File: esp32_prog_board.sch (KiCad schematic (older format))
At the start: 21 parts, among them J1 105450-0101, J2 S6B-PH-SM4-TB, Q1 MMDT2222A, SW1 PTS810, U1 SP3401, U2 AP2112K-3.3, U3 CP2104

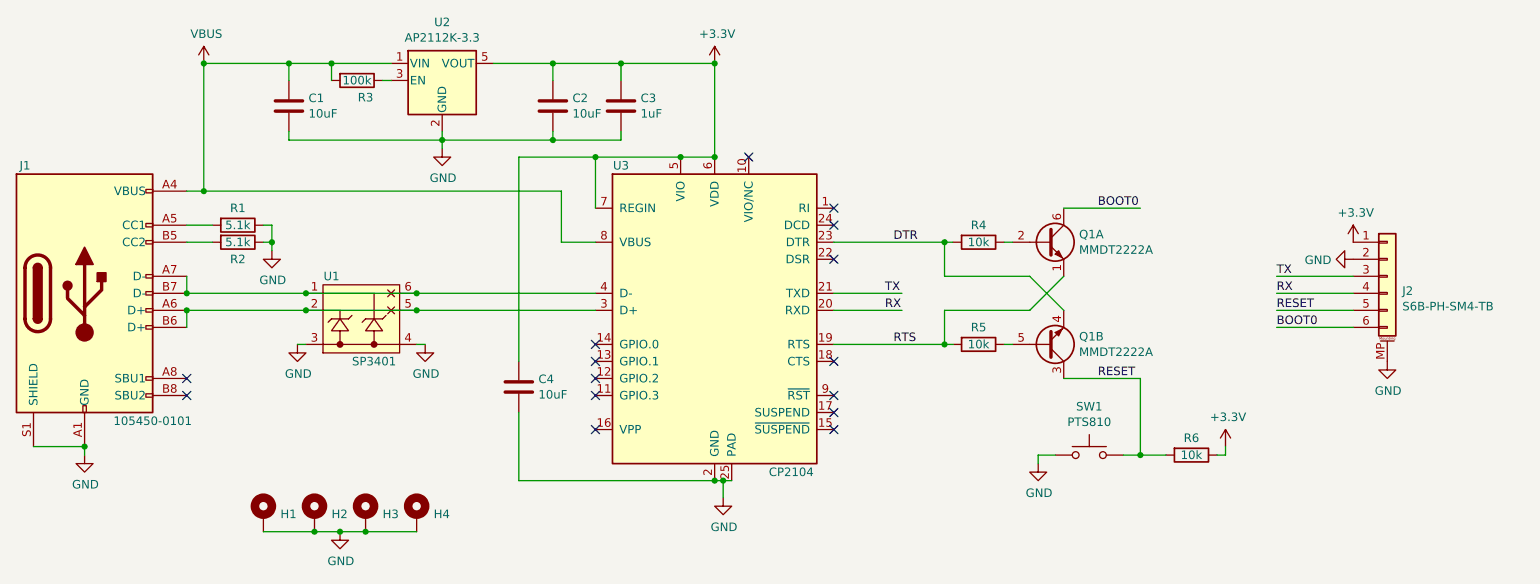
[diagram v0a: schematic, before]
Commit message: Added VBUS ESD, and TX/RX/PWR LEDs
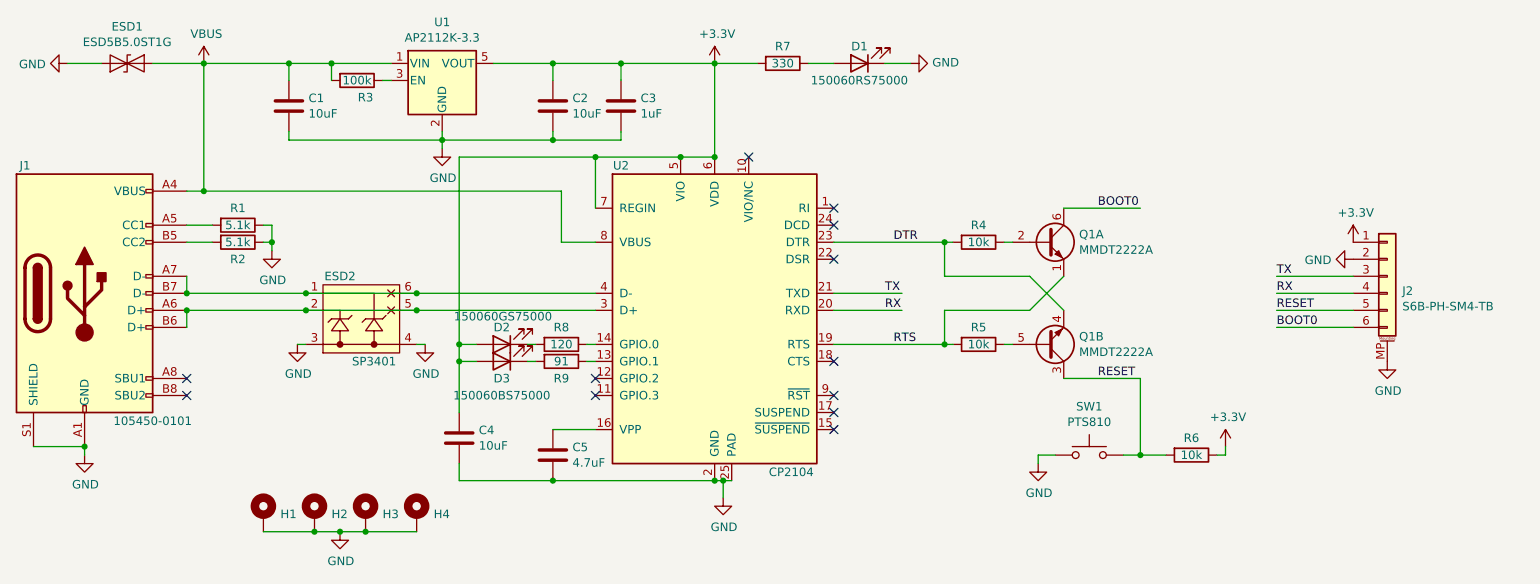
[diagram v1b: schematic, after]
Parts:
- added C5: 4.7uF, Resistor_SMD:R_0603_1608Metric, symbol Device:C
- added D1: 150060RS75000, LED_SMD:LED_0603_1608Metric, symbol Device:LED
- added D2: 150060GS75000, LED_SMD:LED_0603_1608Metric, symbol Device:LED
- added D3: 150060BS75000, LED_SMD:LED_0603_1608Metric, symbol Device:LED
- added ESD1: ESD5B5.0ST1G, Diode_SMD:D_SOD-523, symbol Diode:ESD9B5.0ST5G
- added R7: 330, Resistor_SMD:R_0603_1608Metric, symbol Device:R
- added R8: 120, Resistor_SMD:R_0603_1608Metric, symbol Device:R
- added R9: 91, Resistor_SMD:R_0603_1608Metric, symbol Device:R
- renumbered U1 to ESD2, U2 to U1, U3 to U2
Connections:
- wire segments 84 -> 99
- no-connect marks 15 -> 12
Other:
- moved on the sheet: C4
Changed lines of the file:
@@
 $EndDescr
 $Comp
-L Interface_USB:CP2104 U3
+L Interface_USB:CP2104 U2
 U 1 1 5F29D50C
 P 6000 3750
-F 0 "U3" H 5450 4600 50  0000 C CNN
+F 0 "U2" H 5450 4600 50  0000 C CNN
 F 1 "CP2104" H 6450 2800 50  0000 C CNN
 F 2 "Package_DFN_QFN:QFN-24-1EP_4x4mm_P0.5mm_EP2.6x2.6mm" H 6150 2800 50  0001 L CNN
@@
 NoConn ~ 6700 4350
 NoConn ~ 6700 4450
-NoConn ~ 5300 4450
 NoConn ~ 5300 4250
 NoConn ~ 5300 4150
-NoConn ~ 5300 4050
-NoConn ~ 5300 3950
-$Comp
-L Device:C C4
-U 1 1 5F2B6E8C
-P 4850 4200
-F 0 "C4" H 4965 4246 50  0000 L CNN
-F 1 "10uF" H 4965 4155 50  0000 L CNN
-F 2 "Resistor_SMD:R_0603_1608Metric" H 4888 4050 50  0001 C CNN
-F 3 "~" H 4850 4200 50  0001 C CNN
-	1    4850 4200
-	1    0    0    -1
-$EndComp
-Wire Wire Line
-	4850 4350 4850 4750
-Wire Wire Line
-	4850 4750 6000 4750
 Connection ~ 6000 4750
-Wire Wire Line
-	4850 4050 4850 2850
-Wire Wire Line
-	4850 2850 5300 2850
-Connection ~ 5300 2850
 $Comp
 L power:+3.3V #PWR?
@@
 $EndComp
 Wire Wire Line
-	5100 3050 5100 3350
-Wire Wire Line
-	5100 3350 5300 3350
-Wire Wire Line
 	2900 3050 3000 3050
 Wire Wire Line
 	3000 2300 3000 3050
-Wire Wire Line
-	3000 3050 5100 3050
 Connection ~ 3000 3050
 $Comp
-L LittelFuse:SP3401 U1
+L LittelFuse:SP3401 ESD2
 U 1 1 5F2B5D60
 P 3900 3650
-F 0 "U1" H 3750 3750 50  0000 C CNN
+F 0 "ESD2" H 3800 3750 50  0000 C CNN
 F 1 "SP3401" H 4000 3250 50  0000 C CNN
 F 2 "LittelFuse:SP3401" H 3900 3200 50  0001 C CNN
@@
 RESET
 $Comp
-L Regulator_Linear:AP2112K-3.3 U2
+L Regulator_Linear:AP2112K-3.3 U1
 U 1 1 5F2CF8DA
 P 4400 2400
-F 0 "U2" H 4400 2742 50  0000 C CNN
+F 0 "U1" H 4400 2742 50  0000 C CNN
 F 1 "AP2112K-3.3" H 4400 2651 50  0000 C CNN
 F 2 "Package_TO_SOT_SMD:SOT-23-5" H 4400 2725 50  0001 C CNN
@@
 Wire Wire Line
 	9300 3850 9750 3850
+Connection ~ 5300 2850
+Wire Wire Line
+	3000 3050 5100 3050
+Wire Wire Line
+	5100 3350 5300 3350
+Wire Wire Line
+	5100 3050 5100 3350
+$Comp
+L Device:C C4
+U 1 1 5F2B6E8C
+P 4500 4500
+F 0 "C4" H 4615 4546 50  0000 L CNN
+F 1 "10uF" H 4615 4455 50  0000 L CNN
+F 2 "Resistor_SMD:R_0603_1608Metric" H 4538 4350 50  0001 C CNN
+F 3 "~" H 4500 4500 50  0001 C CNN
+	1    4500 4500
+	1    0    0    -1
+$EndComp
+Wire Wire Line
+	4500 4650 4500 4750
+Wire Wire Line
+	4500 4350 4500 4050
+Wire Wire Line
+	4500 2850 5300 2850
+$Comp
+L Device:C C5
+U 1 1 5F2F6677
+P 5050 4600
+F 0 "C5" H 5165 4646 50  0000 L CNN
+F 1 "4.7uF" H 5165 4555 50  0000 L CNN
+F 2 "Resistor_SMD:R_0603_1608Metric" H 5088 4450 50  0001 C CNN
+F 3 "~" H 5050 4600 50  0001 C CNN
+	1    5050 4600
+	1    0    0    -1
+$EndComp
+Wire Wire Line
+	4500 4750 5050 4750
+Wire Wire Line
+	5050 4750 6000 4750
+Connection ~ 5050 4750
+Wire Wire Line
+	5050 4450 5300 4450
+$Comp
+L Diode:ESD9B5.0ST5G ESD1
+U 1 1 5F2A4472
+P 2550 2300
+F 0 "ESD1" H 2550 2516 50  0000 C CNN
+F 1 "ESD5B5.0ST1G" H 2550 2425 50  0000 C CNN
+F 2 "Diode_SMD:D_SOD-523" H 2550 2300 50  0001 C CNN
+F 3 "" H 2550 2300 50  0001 C CNN
+	1    2550 2300
+	1    0    0    -1
+$EndComp
+$Comp
+L power:GND #PWR?
+U 1 1 5F2AC941
+P 2200 2300
+F 0 "#PWR?" H 2200 2050 50  0001 C CNN
+F 1 "GND" V 2205 2172 50  0000 R CNN
+F 2 "" H 2200 2300 50  0001 C CNN
+F 3 "" H 2200 2300 50  0001 C CNN
+	1    2200 2300
+	0    1    1    0
+$EndComp
+Wire Wire Line
+	2200 2300 2400 2300
+Wire Wire Line
+	2700 2300 3000 2300
+$Comp
+L Device:R R7
+U 1 1 5F2B9ABB
+P 6400 2300
+F 0 "R7" V 6300 2300 50  0000 C CNN
+F 1 "330" V 6400 2300 50  0000 C CNN
+F 2 "Resistor_SMD:R_0603_1608Metric" V 6330 2300 50  0001 C CNN
+F 3 "~" H 6400 2300 50  0001 C CNN
+	1    6400 2300
+	0    1    1    0
+$EndComp
+$Comp
+L Device:R R8
+U 1 1 5F2BA0DD
+P 5100 3950
+F 0 "R8" V 5000 3950 50  0000 C CNN
+F 1 "120" V 5100 3950 50  0000 C CNN
+F 2 "Resistor_SMD:R_0603_1608Metric" V 5030 3950 50  0001 C CNN
+F 3 "~" H 5100 3950 50  0001 C CNN
+	1    5100 3950
+	0    1    1    0
+$EndComp
+$Comp
+L Device:R R9
+U 1 1 5F2BA7D1
+P 5100 4050
+F 0 "R9" V 5200 4050 50  0000 C CNN
+F 1 "91" V 5100 4050 50  0000 C CNN
+F 2 "Resistor_SMD:R_0603_1608Metric" V 5030 4050 50  0001 C CNN
+F 3 "~" H 5100 4050 50  0001 C CNN
+	1    5100 4050
+	0    1    1    0
+$EndComp
+Wire Wire Line
+	6000 2300 6250 2300
+$Comp
+L Device:LED D1
+U 1 1 5F2C4AFE
+P 6850 2300
+F 0 "D1" H 6850 2200 50  0000 C CNN
+F 1 "150060RS75000" H 6850 2400 50  0000 C CNN
+F 2 "LED_SMD:LED_0603_1608Metric" H 6850 2300 50  0001 C CNN
+F 3 "~" H 6850 2300 50  0001 C CNN
+	1    6850 2300
+	-1   0    0    1
+$EndComp
+$Comp
+L power:GND #PWR?
+U 1 1 5F2C65F7
+P 7150 2300
+F 0 "#PWR?" H 7150 2050 50  0001 C CNN
+F 1 "GND" V 7155 2172 50  0000 R CNN
+F 2 "" H 7150 2300 50  0001 C CNN
+F 3 "" H 7150 2300 50  0001 C CNN
+	1    7150 2300
+	0    -1   -1   0
+$EndComp
+Wire Wire Line
+	6550 2300 6700 2300
+Wire Wire Line
+	7000 2300 7150 2300
+Wire Wire Line
+	5250 3950 5300 3950
+Wire Wire Line
+	5250 4050 5300 4050
+$Comp
+L Device:LED D2
+U 1 1 5F2DAF7D
+P 4750 3950
+F 0 "D2" H 4750 3850 50  0000 C CNN
+F 1 "150060GS75000" H 4743 3786 50  0000 C CNN
+F 2 "LED_SMD:LED_0603_1608Metric" H 4750 3950 50  0001 C CNN
+F 3 "~" H 4750 3950 50  0001 C CNN
+	1    4750 3950
+	-1   0    0    1
+$EndComp
+$Comp
+L Device:LED D3
+U 1 1 5F2DB7FA
+P 4750 4050
+F 0 "D3" H 4750 4150 50  0000 C CNN
+F 1 "150060BS75000" H 4750 4250 50  0000 C CNN
+F 2 "LED_SMD:LED_0603_1608Metric" H 4750 4050 50  0001 C CNN
+F 3 "~" H 4750 4050 50  0001 C CNN
+	1    4750 4050
+	-1   0    0    1
+$EndComp
+Wire Wire Line
+	4600 3950 4500 3950
+Connection ~ 4500 3950
+Wire Wire Line
+	4500 3950 4500 2850
+Wire Wire Line
+	4600 4050 4500 4050
+Connection ~ 4500 4050
+Wire Wire Line
+	4500 4050 4500 3950
+Wire Wire Line
+	4900 3950 4950 3950
+Wire Wire Line
+	4900 4050 4950 4050
 $EndSCHEMATC

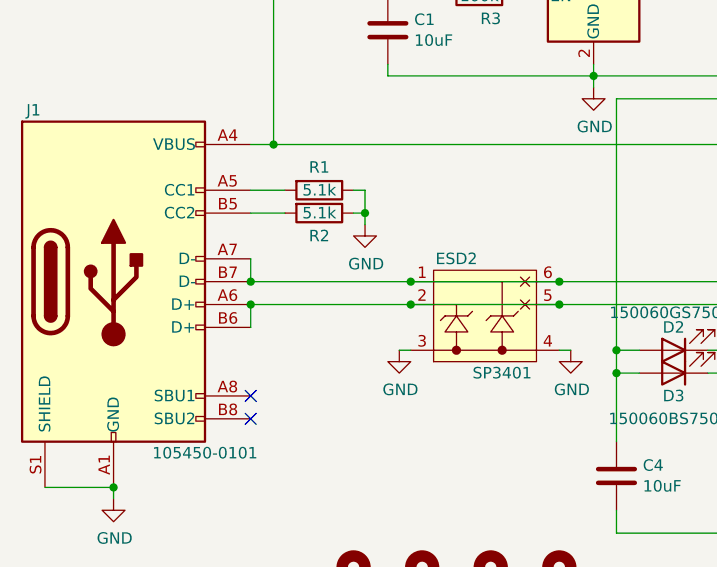
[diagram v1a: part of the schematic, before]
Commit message: Completed routing
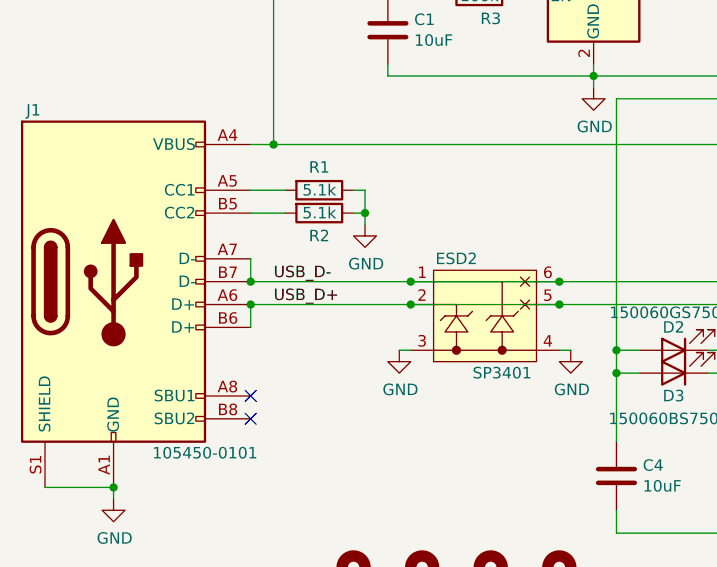
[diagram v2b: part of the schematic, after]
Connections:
- net labels added: USB_D+, USB_D-
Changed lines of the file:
@@
 Wire Wire Line
 	4900 4050 4950 4050
+Text Label 3000 3650 0    50   ~ 0
+USB_D-
+Text Label 3000 3750 0    50   ~ 0
+USB_D+
 $EndSCHEMATC
